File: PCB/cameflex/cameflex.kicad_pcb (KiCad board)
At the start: 2 copper layers, 33 parts, among them J1 ESP32-C3_Left, J2 ESP32-C3_Right, J3 CON5_HALL, Q1 JY317P, U1 JY01(8559), U3 JY213L

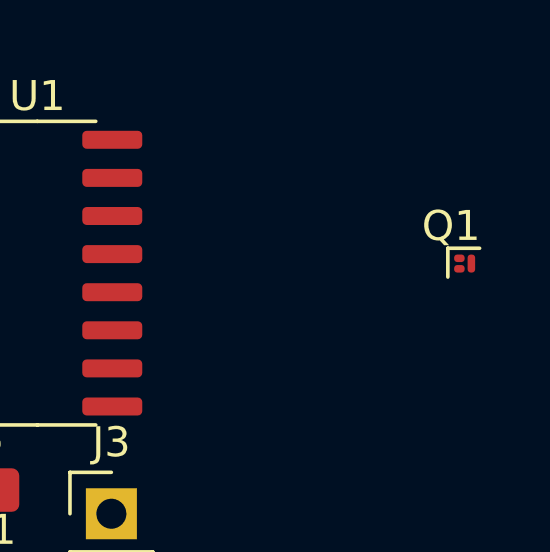
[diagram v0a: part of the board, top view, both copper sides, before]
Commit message: Chore: sync PCB cache and cleanup archived tuning assets
- Update .gitignore (note.txt, memory.db-*)
- Sync KiCad fp-info-cache and schematic/pcb whitespace
- Remove archived auto_tune bundle (superseded by current control)

Co-authored-by: Mema <mema@glassgallery.my.id>
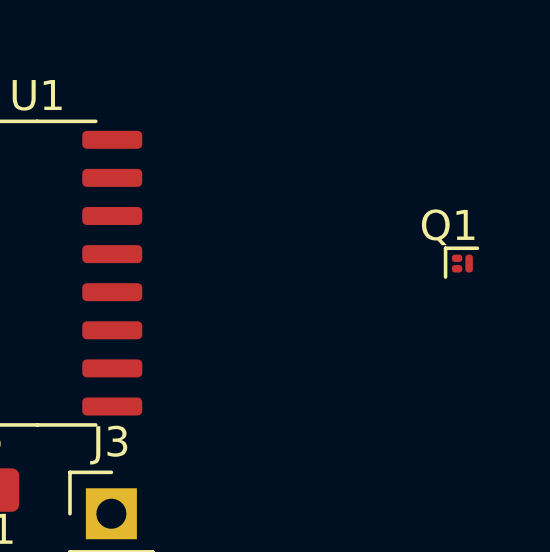
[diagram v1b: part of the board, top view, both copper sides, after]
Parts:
- moved Q1 0.08 mm to (115.2, 70.5)
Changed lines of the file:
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@@
 	(footprint "Package_DFN_QFN:Texas_PicoStar_DFN-3_0.69x0.60mm"
 		(layer "F.Cu")
-		(at 115.275 70.5)
+		(at 115.2 70.5)
 		(descr "Texas Picostar DFN-3, 0.73x0.64mm max, 0.69x0.60mm nom, https://www.ti.com/lit/ds/symlink/csd13380f3.pdf")
 		(tags "TI YJM0003A")
